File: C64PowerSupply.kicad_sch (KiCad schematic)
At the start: 22 parts, among them J1 120V IN, J2 OUT, U1 LM2596T-ADJ

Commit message: wip
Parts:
- removed C2: 2200μF, Capacitor_THT:CP_Radial_D18.0mm_P7.50mm, symbol Device:C_Polarized
- removed D2: SK33A-TP, DTLib:DO-214AC, symbol Device:D_Schottky
- removed HS1: Heatsink, DTLib:AAVID581002B02500G, symbol Mechanical:Heatsink
- removed U1: LM2596T-ADJ, Package_TO_SOT_THT:TO-220-5_P3.4x3.7mm_StaggerOdd_Lead3.8mm_Vertical, symbol Regulator_Switching:LM2596T-ADJ
- added C2: 0.1μF, Capacitor_SMD:C_0805_2012Metric_Pad1.18x1.45mm_HandSolder, symbol Device:C
- added C6: 22μF, Capacitor_SMD:C_1210_3225Metric_Pad1.33x2.70mm_HandSolder, symbol Device:C
- added R1: 1M, Resistor_THT:R_Axial_DIN0414_L11.9mm_D4.5mm_P15.24mm_Horizontal, symbol Device:R
- added RV2: MOV, Varistor:RV_Disc_D9mm_W4mm_P5mm, symbol Device:Varistor
- added RV3, RV4: TVS, Diode_SMD:D_SMB_Handsoldering, symbol Device:Varistor
- added SW1: 120/240V SELECT, Button_Switch_THT:SW_E-Switch_EG1271_DPDT, symbol Switch:SW_DPDT_x2
- added U1: BD9E303EFJ-LBE2, Package_SO:HTSOP-8-1EP_3.9x4.9mm_P1.27mm_EP2.4x3.2mm_ThermalVias, symbol DTLib:BD9E303EFJ-LBE2
- C5: value 220μF -> 22μF; footprint Capacitor_THT:CP_Radial_D8.0mm_P3.50mm -> Capacitor_SMD:C_1210_3225Metric_Pad1.33x2.70mm_HandSolder; symbol Device:C_Polarized -> Device:C
- F2: value 1.5A -> 2.5A
- L1: value 33μH -> 10μH; footprint DTLib:L_Bourns-SRN1060 -> DTLib:L_BMRx00060630
- TR1: value 2x115V to 2x9V -> 2x115V to 2x8V; footprint DTLib:Transformer_L01_60x60 -> DTLib:Transformer_Hammond_183K16; symbol Transformer:TRANSF6 -> DTLib:Transformer_Hammond_183
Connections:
- net 9VAC+: now also F1.2, TR1.7, RV3.1; no longer F1.1, J2.1 (Pin_1)
- net 9VAC-: now also TR1.9, RV3.2; no longer TR1.7
- net GND: now also C2.2, C6.2
- net VCC: now also F2.2, C6.1; no longer J2.3 (Pin_3)
- net VUNREG: now also C2.1
- net at D1.2: now also TR1.12, RV4.2; no longer TR1.5
- net AC_HOT: now reaches TR1.6
- net AC_HOT: now also C1.1, J1.1 (Pin_1), R1.1, RV2.1, SW1.4 (A); no longer F2.2
- net at D1.4: now also TR1.10, RV4.1; no longer F2.1
- removed net HOT: C1.1, J1.1 (Pin_1), TR1.1, TR1.3
- net NEUTRAL renamed AC_NEUTRAL
- net AC_NEUTRAL: now also TR1.1, R1.2, RV2.2, SW1.1 (A); no longer TR1.2, TR1.4
- new net: SW1.5 (B), TR1.3
- new net: SW1.2 (B), TR1.4
- new net: SW1.3 (C), SW1.6 (C)
- new net F_9VAC+: F1.1, J2.1 (Pin_1)
- new net F_VCC: F2.1, J2.3 (Pin_3)
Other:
- note added: "9VAC+ 9VAC- +5VDC GND"
- note added: "TR1: 183K16 - PWR XFMR LAMINATED 56VA RV3,RV4: SMBJP6KE15CA-TP - TVS DIODE 12.8VWM L1: BMRF00060630100MA1 - FIXED IND 10UH 4A C5,C6: CER 22UF 25V X7R 1210"
- title: C64 Power Supply -> C64/C128 Power Supply
- moved on the sheet: C1, C3, C4, D1, F1, F2, J1, J2, L1

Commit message: Begin route
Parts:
- removed C4: 100μF, Capacitor_THT:CP_Radial_D8.0mm_P3.50mm, symbol Device:C_Polarized
- added C3: 10μF, Capacitor_SMD:C_1206_3216Metric_Pad1.33x1.80mm_HandSolder, symbol Device:C
- added C5: 6800pF, Capacitor_SMD:C_0805_2012Metric_Pad1.18x1.45mm_HandSolder, symbol Device:C_Small
- added C6: 0.1μF, Capacitor_SMD:C_0805_2012Metric_Pad1.18x1.45mm_HandSolder, symbol Device:C_Small
- added J3: OUT C128, TerminalBlock_Phoenix:TerminalBlock_Phoenix_PT-1,5-4-5.0-H_1x04_P5.00mm_Horizontal, symbol Connector:Screw_Terminal_01x04
- added JP1: GND LINK, Jumper:SolderJumper-2_P1.3mm_Bridged_Pad1.0x1.5mm, symbol Jumper:Jumper_2_Bridged
- J2: value OUT -> OUT C64
- R1: value 1M -> 15K; footprint Resistor_THT:R_Axial_DIN0414_L11.9mm_D4.5mm_P15.24mm_Horizontal -> Resistor_SMD:R_0805_2012Metric_Pad1.20x1.40mm_HandSolder
- R2: value 1K8 -> 22K
- R3: value 1K -> 5.6K
- RV2: renamed from RV3; footprint Diode_SMD:D_SMB_Handsoldering -> Diode_SMD:D_SMB
- RV3: renamed from RV4; footprint Diode_SMD:D_SMB_Handsoldering -> Diode_SMD:D_SMB
- RV4: renamed from RV1; footprint Potentiometer_THT:Potentiometer_Bourns_3266W_Vertical -> Potentiometer_THT:Potentiometer_Bourns_3296W_Vertical
- SW1: footprint Button_Switch_THT:SW_E-Switch_EG1271_DPDT -> Button_Switch_THT:SW_NKK_G1xJP
- U1: footprint Package_SO:HTSOP-8-1EP_3.9x4.9mm_P1.27mm_EP2.4x3.2mm_ThermalVias -> Package_SO:Texas_HTSOP-8-1EP_3.9x4.9mm_P1.27mm_EP2.95x4.9mm_Mask2.4x3.1mm_ThermalVias
- renumbered C3 to C2, C2 to C4, C5 to C7, C6 to C8, RV2 to RV1
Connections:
- net REG-OUT is gone; now on net REG-SW: L1.1
- net AC_HOT: no longer R1.1
- net AC_NEUTRAL: no longer R1.2
- net GND: now also R1.2, U1.4 (AGND), U1.7 (PGND), U1.9 (EPAD), C3.2, J3.4 (Pin_4), JP1.2 (B); no longer J1.3 (Pin_3)
- net VUNREG: now also U1.2 (VIN), U1.3 (EN), C3.1
- net at RV3.1, TR1.10: now also F2.2; no longer D1.4
- net BOOT: now reaches U1.1 (BOOT)
- net BOOT: now also C6.1
- net COMP: now reaches U1.6 (COMP)
- net COMP: now also C5.2
- net REG-SW: now reaches U1.8 (SW)
- net REG-SW: now also C6.2
- net 9VAC+: no longer names the net of F1.2, RV2.1, TR1.7
- net 9VAC- renamed 9VAC_B
- net 9VAC_B: now also J3.2 (Pin_2)
- net F_9VAC+ renamed 9VAC_A
- net 9VAC_A: now also J3.1 (Pin_1)
- net F_VCC: no longer names the net of F2.1
- net F_VCC: now also D1.4; no longer J2.3 (Pin_3)
- net VADJ renamed FB
- net FB: now also U1.5 (FB)
- net VCC renamed 5VDC
- net 5VDC: now also J2.3 (Pin_3), J3.3 (Pin_3); no longer F2.2
- new net: C5.1, R1.1
- new net Earth: J1.3 (Pin_3), JP1.1 (A)
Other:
- note added: "AC Ground link MUST be connected if case is metal. Transformer provides isolation so link can be broken if experiencing ground loop/noise issues"
- note added: "Optional, can be left out"
- note added: "TR1: 183K16 - PWR XFMR LAMINATED 56VA D1: KBPC610-A1-0000 1000V 6A RV2,RV3: SMBJP6KE15CA-TP - TVS DIODE 12.8VWM L1: BMRF00060630100MA1 - FIXED IND 10UH 4A C1: CAP FILM 0.047UF 20% 560VDC RAD C2: CAP ALUM 1000UF 20% 50V RADIAL 105°C C3: CER 10UF 25V X7R 1206 C4,C6: CER 0.1UF 25V X7R 0805 C7,C8: CER 22UF 25V X7R 1210"
- note added: "VCC Range (Vout = (R2+R3)/R3 x 1.0V) MIN (RV1=0R): R2 = 22K, R3 = 5.6K, Vout = 4.93V MAX (RV1=2K): R2 = 24K, R3 = 5.6K, Vout = 5.28V"
- note removed: "9VAC+ 9VAC- +5VDC GND"
- note removed: "TR1: 183K16 - PWR XFMR LAMINATED 56VA RV3,RV4: SMBJP6KE15CA-TP - TVS DIODE 12.8VWM L1: BMRF00060630100MA1 - FIXED IND 10UH 4A C5,C6: CER 22UF 25V X7R 1210"
- moved on the sheet: C1, C2, C4, C7, C8, F1, J2, L1, R2, R3, RV4

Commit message: Cleanup, fix 120/240V switch
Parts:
- SW1: footprint Button_Switch_THT:SW_NKK_G1xJP -> Button_Switch_THT:SW_NKK_GW12LJP
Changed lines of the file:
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@@
       (effects (font (size 1.27 1.27)) hide)
     )
-    (property "Footprint" "Button_Switch_THT:SW_NKK_G1xJP" (id 2) (at 38.1 74.93 0)
+    (property "Footprint" "Button_Switch_THT:SW_NKK_GW12LJP" (id 2) (at 38.1 74.93 0)
       (effects (font (size 1.27 1.27)) hide)
     )
@@
     (property "Reference" "SW1" (id 0) (at 39.37 58.42 0))
     (property "Value" "120/240V SELECT" (id 1) (at 38.1 60.96 0))
-    (property "Footprint" "Button_Switch_THT:SW_NKK_G1xJP" (id 2) (at 38.1 66.04 0)
+    (property "Footprint" "Button_Switch_THT:SW_NKK_GW12LJP" (id 2) (at 38.1 66.04 0)
       (effects (font (size 1.27 1.27)) hide)
     )
@@
     )
     (path "/9cf55ed4-dd28-4f74-a0dd-663e350a82d3"
-      (reference "SW1") (unit 1) (value "120/240V SELECT") (footprint "Button_Switch_THT:SW_NKK_G1xJP")
+      (reference "SW1") (unit 1) (value "120/240V SELECT") (footprint "Button_Switch_THT:SW_NKK_GW12LJP")
     )
     (path "/0ee86955-6c93-4014-949a-24fd577f7e5a"
-      (reference "SW1") (unit 2) (value "120/240V SELECT") (footprint "Button_Switch_THT:SW_NKK_G1xJP")
+      (reference "SW1") (unit 2) (value "120/240V SELECT") (footprint "Button_Switch_THT:SW_NKK_GW12LJP")
     )
     (path "/00000000-0000-0000-0000-000060cfadc3"

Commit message: Voltage sel switch footprint
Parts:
- RV1: footprint Varistor:RV_Disc_D9mm_W4mm_P5mm -> Varistor:RV_Disc_D15.5mm_W3.9mm_P7.5mm
- SW1: footprint Button_Switch_THT:SW_NKK_GW12LJP -> DTLib:V_SEL_SWITCH
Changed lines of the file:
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@@
       (effects (font (size 1.27 1.27)) hide)
     )
-    (property "Footprint" "Button_Switch_THT:SW_NKK_GW12LJP" (id 2) (at 38.1 74.93 0)
+    (property "Footprint" "DTLib:V_SEL_SWITCH" (id 2) (at 38.1 74.93 0)
       (effects (font (size 1.27 1.27)) hide)
     )
@@
       (effects (font (size 1.27 1.27)) (justify left))
     )
-    (property "Footprint" "Varistor:RV_Disc_D9mm_W4mm_P5mm" (id 2) (at 42.672 30.48 90)
+    (property "Footprint" "Varistor:RV_Disc_D15.5mm_W3.9mm_P7.5mm" (id 2) (at 42.672 30.48 90)
       (effects (font (size 1.27 1.27)) hide)
     )
@@
     (property "Reference" "SW1" (id 0) (at 39.37 58.42 0))
     (property "Value" "120/240V SELECT" (id 1) (at 38.1 60.96 0))
-    (property "Footprint" "Button_Switch_THT:SW_NKK_GW12LJP" (id 2) (at 38.1 66.04 0)
+    (property "Footprint" "DTLib:V_SEL_SWITCH" (id 2) (at 38.1 66.04 0)
       (effects (font (size 1.27 1.27)) hide)
     )
@@
     )
     (path "/6e157920-730e-4541-9e46-a28abfb26597"
-      (reference "RV1") (unit 1) (value "MOV") (footprint "Varistor:RV_Disc_D9mm_W4mm_P5mm")
+      (reference "RV1") (unit 1) (value "MOV") (footprint "Varistor:RV_Disc_D15.5mm_W3.9mm_P7.5mm")
     )
     (path "/93a3a40d-d02c-457c-87cb-b4cffa2e3ae1"
@@
     )
     (path "/9cf55ed4-dd28-4f74-a0dd-663e350a82d3"
-      (reference "SW1") (unit 1) (value "120/240V SELECT") (footprint "Button_Switch_THT:SW_NKK_GW12LJP")
+      (reference "SW1") (unit 1) (value "120/240V SELECT") (footprint "DTLib:V_SEL_SWITCH")
     )
     (path "/0ee86955-6c93-4014-949a-24fd577f7e5a"
-      (reference "SW1") (unit 2) (value "120/240V SELECT") (footprint "Button_Switch_THT:SW_NKK_GW12LJP")
+      (reference "SW1") (unit 2) (value "120/240V SELECT") (footprint "DTLib:V_SEL_SWITCH")
     )
     (path "/00000000-0000-0000-0000-000060cfadc3"

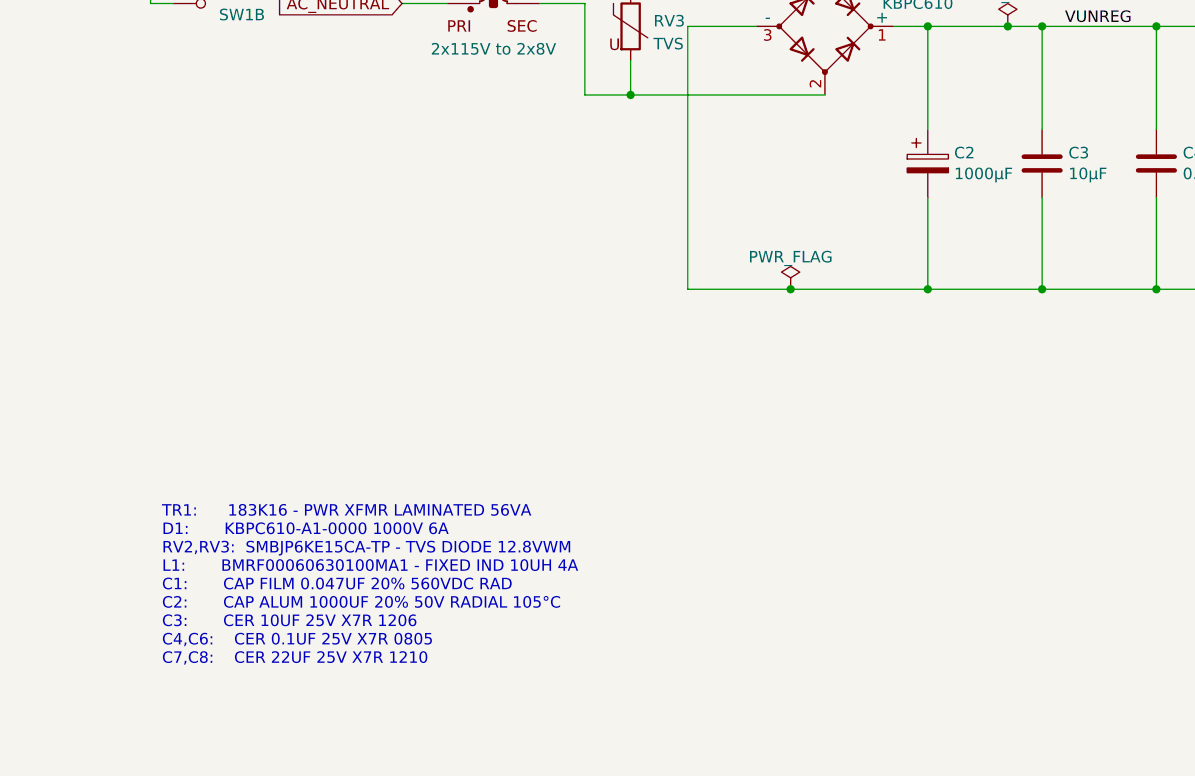
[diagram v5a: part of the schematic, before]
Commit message: Bumped C2 to 2200uF
1000uF worked fine @ 2A but regulation dropped quickly after
because ripple was too large. 2200uF is enough to go up to 3A.
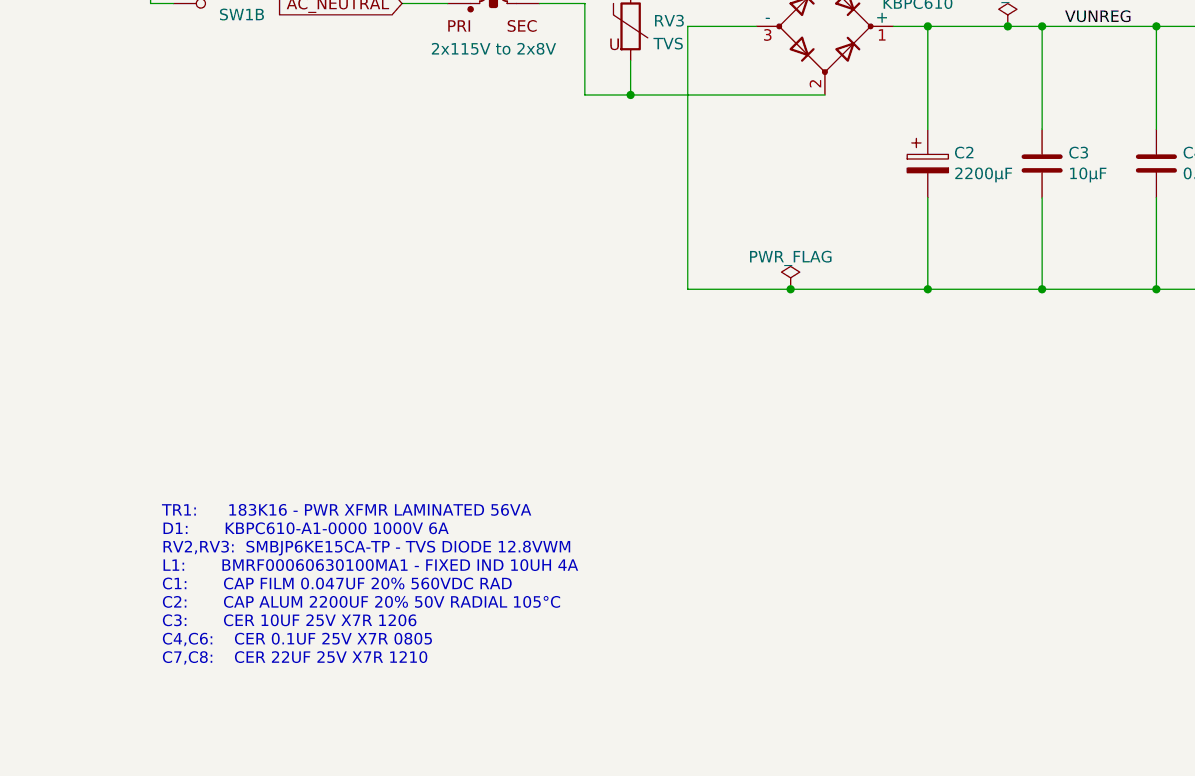
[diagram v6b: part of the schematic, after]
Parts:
- C2: value 1000μF -> 2200μF
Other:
- note added: "TR1: 183K16 - PWR XFMR LAMINATED 56VA D1: KBPC610-A1-0000 1000V 6A RV2,RV3: SMBJP6KE15CA-TP - TVS DIODE 12.8VWM L1: BMRF00060630100MA1 - FIXED IND 10UH 4A C1: CAP FILM 0.047UF 20% 560VDC RAD C2: CAP ALUM 2200UF 20% 50V RADIAL 105°C C3: CER 10UF 25V X7R 1206 C4,C6: CER 0.1UF 25V X7R 0805 C7,C8: CER 22UF 25V X7R 1210"
- note removed: "TR1: 183K16 - PWR XFMR LAMINATED 56VA D1: KBPC610-A1-0000 1000V 6A RV2,RV3: SMBJP6KE15CA-TP - TVS DIODE 12.8VWM L1: BMRF00060630100MA1 - FIXED IND 10UH 4A C1: CAP FILM 0.047UF 20% 560VDC RAD C2: CAP ALUM 1000UF 20% 50V RADIAL 105°C C3: CER 10UF 25V X7R 1206 C4,C6: CER 0.1UF 25V X7R 0805 C7,C8: CER 22UF 25V X7R 1210"
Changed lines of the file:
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@@
   (title_block
     (title "C64/C128 Power Supply")
-    (date "2022-09-17")
+    (date "2022-09-23")
     (rev "B")
   )
@@
     (effects (font (size 1.27 1.27)) (justify left bottom))
   )
-  (text "TR1:      183K16 - PWR XFMR LAMINATED 56VA\nD1:       KBPC610-A1-0000 1000V 6A\nRV2,RV3:  SMBJP6KE15CA-TP - TVS DIODE 12.8VWM \nL1:       BMRF00060630100MA1 - FIXED IND 10UH 4A\nC1:       CAP FILM 0.047UF 20% 560VDC RAD\nC2:       CAP ALUM 1000UF 20% 50V RADIAL 105°C\nC3:       CER 10UF 25V X7R 1206\nC4,C6:    CER 0.1UF 25V X7R 0805\nC7,C8:    CER 22UF 25V X7R 1210\n"
+  (text "TR1:      183K16 - PWR XFMR LAMINATED 56VA\nD1:       KBPC610-A1-0000 1000V 6A\nRV2,RV3:  SMBJP6KE15CA-TP - TVS DIODE 12.8VWM \nL1:       BMRF00060630100MA1 - FIXED IND 10UH 4A\nC1:       CAP FILM 0.047UF 20% 560VDC RAD\nC2:       CAP ALUM 2200UF 20% 50V RADIAL 105°C\nC3:       CER 10UF 25V X7R 1206\nC4,C6:    CER 0.1UF 25V X7R 0805\nC7,C8:    CER 22UF 25V X7R 1210\n"
     (at 31.75 151.13 0)
     (effects (font (size 1.27 1.27)) (justify left bottom))
@@
       (effects (font (size 1.27 1.27)) (justify left))
     )
-    (property "Value" "1000μF" (id 1) (at 119.761 96.393 0)
+    (property "Value" "2200μF" (id 1) (at 119.761 96.393 0)
       (effects (font (size 1.27 1.27)) (justify left))
     )
@@
     )
     (path "/00000000-0000-0000-0000-000060d15bdb"
-      (reference "C2") (unit 1) (value "1000μF") (footprint "Capacitor_THT:CP_Radial_D16.0mm_P7.50mm")
+      (reference "C2") (unit 1) (value "2200μF") (footprint "Capacitor_THT:CP_Radial_D16.0mm_P7.50mm")
     )
     (path "/7254fb60-50d3-4b7a-9a31-2a919d8e6e76"
